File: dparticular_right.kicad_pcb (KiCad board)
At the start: 2 copper layers, 51 parts, among them J1 To Left Hand, SW1:10 Key_Ins, SW1:11 Key_Prnt, SW2:10 Key_F7, SW2:11 Key_F8, SW2:12 Key_F9, SW2:13 Key_F10, SW2:14 Key_F11, SW2:15 Key_F12, SW2:16 Key_Del, SW3:10 Key_7, SW3:11 Key_8, SW3:12 Key_9, SW3:13 Key_0, SW3:14 Key_Hyph, SW3:15 Key_Eql, SW3:16 Key_Bksp, SW3:9 Key_6, SW4:10 Key_U, SW4:11 Key_I, SW4:12 Key_O, SW4:13 Key_P, SW4:14 Key_LBrk, SW4:15 Key_RBrk, SW4:16 Key_BkSl, SW4:9 Key_Y, SW5:10 Key_J, SW5:11 Key_K, SW5:12 Key_L, SW5:13 Key_Semi, SW5:14 Key_Quot, SW5:16 Key_Entr, SW5:9 Key_H, SW6:10 Key_M, SW6:11 Key_Coma, SW6:12 Key_Per, SW6:13 Key_Slsh, SW6:14 Key_RShft, SW6:9 Key_N, SW7:11 Key_RAlt, SW7:12 Key_RWin, SW7:13 Key_Menu, SW7:14 Key_RCtrl, SW7:9 Key_RSpc, U1 MCP23018

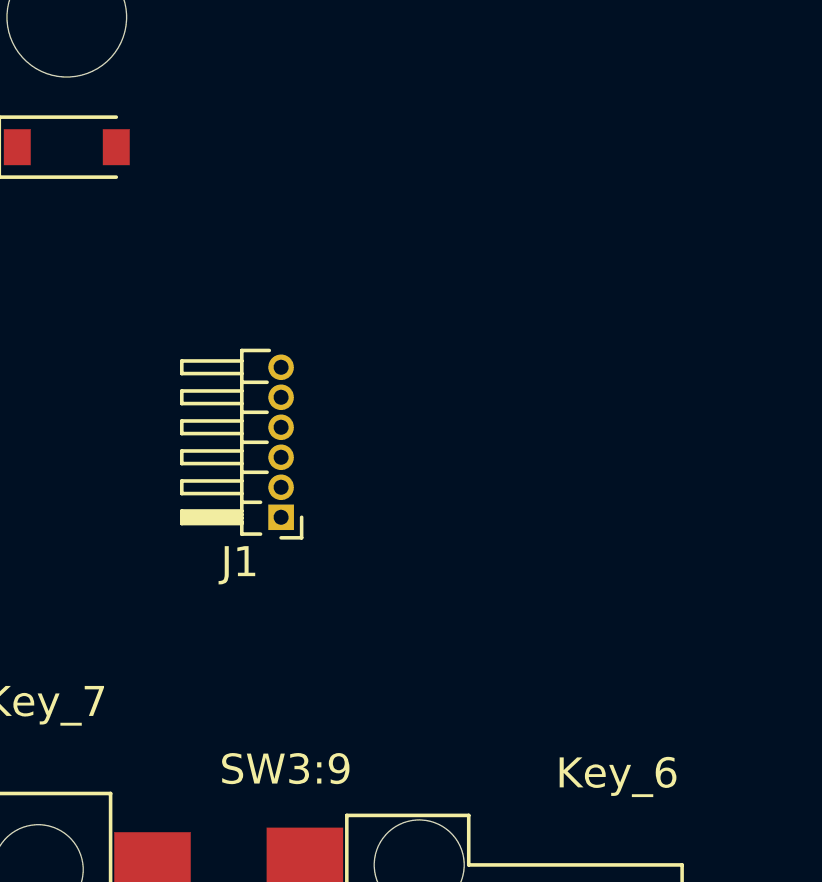
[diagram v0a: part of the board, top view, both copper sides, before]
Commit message: Fixed footprints on switches and headers
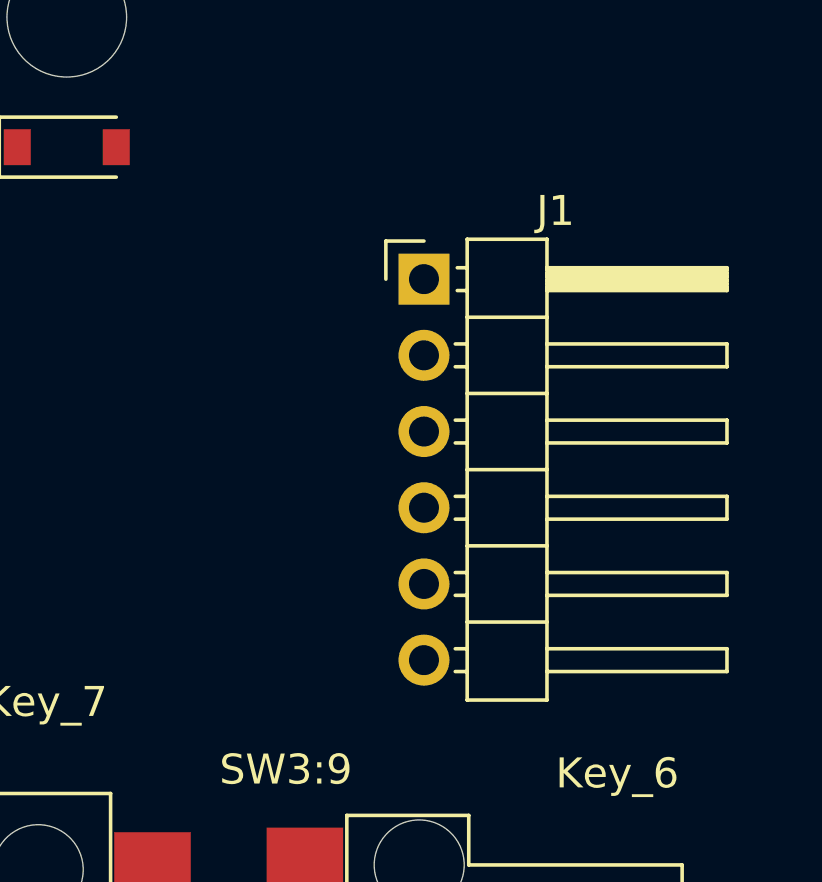
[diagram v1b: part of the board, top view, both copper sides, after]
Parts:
- J1: footprint Connector_PinHeader_1.00mm:PinHeader_1x06_P1.00mm_Horizontal -> Connector_PinHeader_2.54mm:PinHeader_1x06_P2.54mm_Horizontal
- moved J1 9.26 mm to (188.1, 65.9), turned to 0 degrees

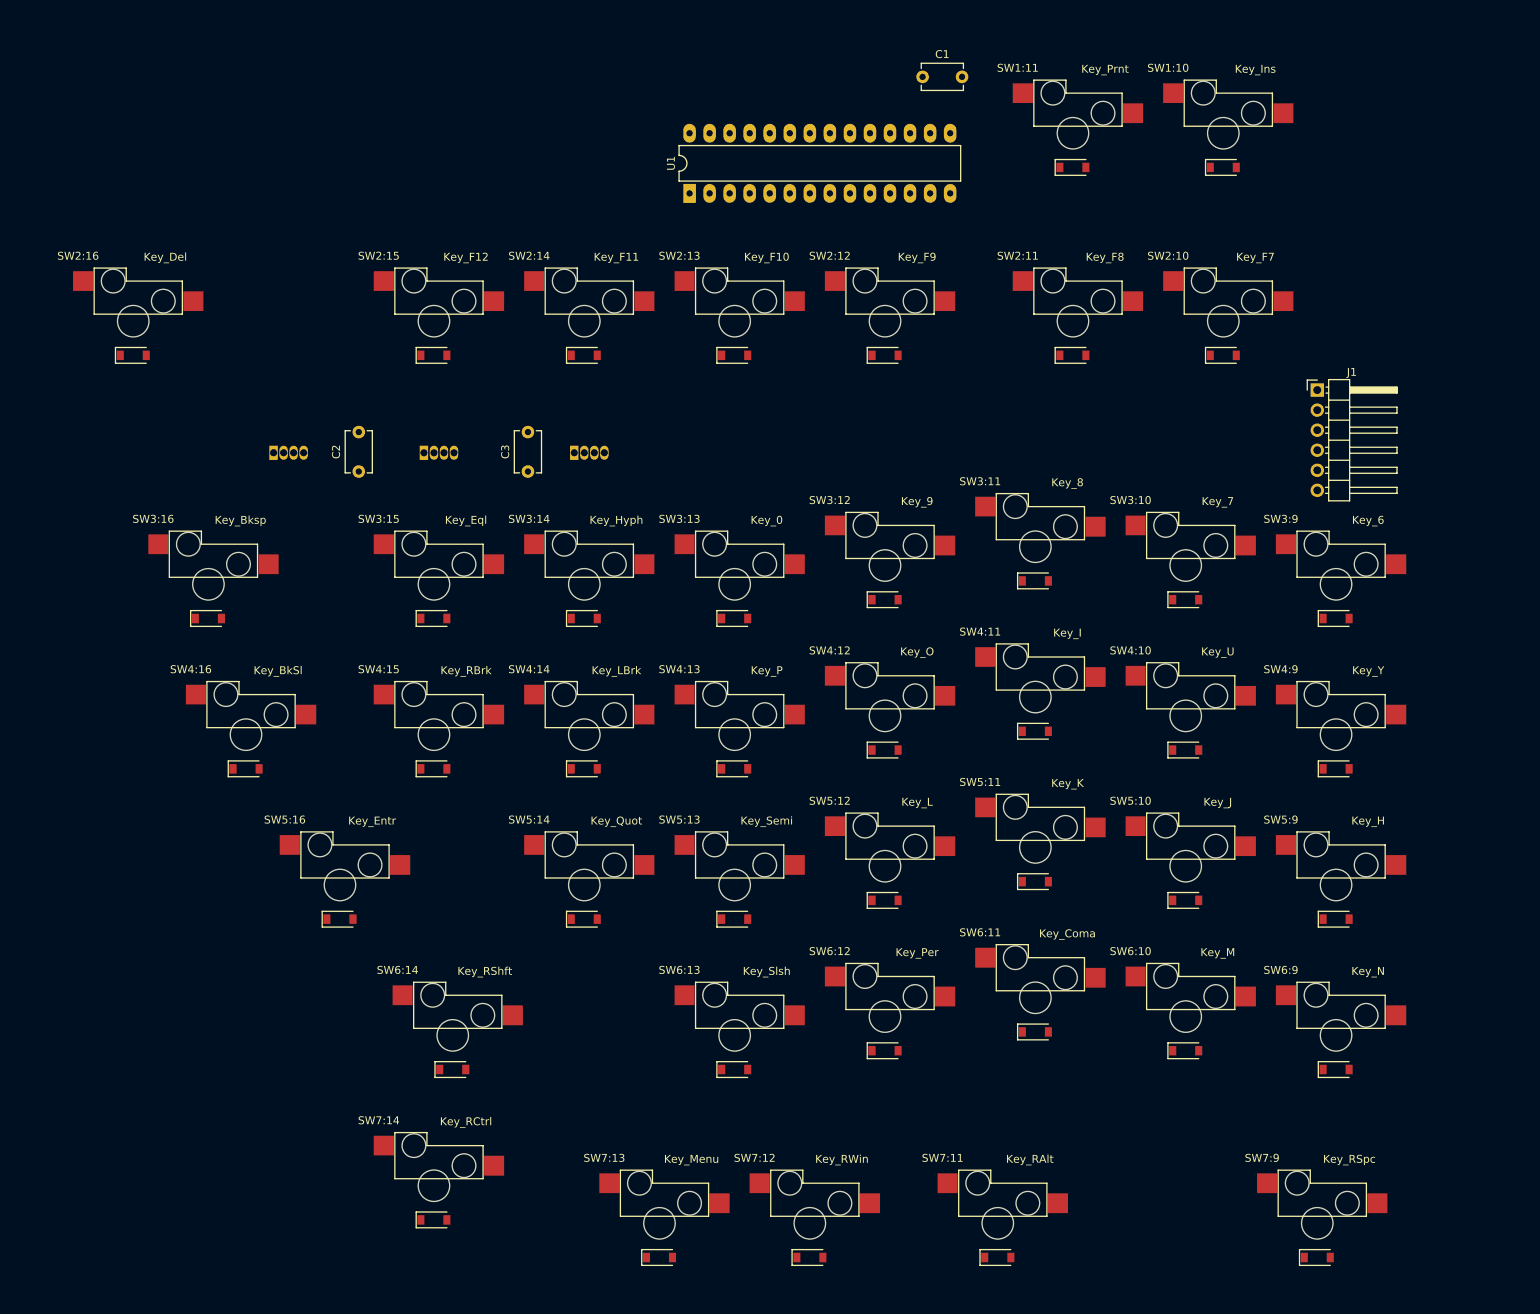
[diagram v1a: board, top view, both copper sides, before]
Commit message: Edge cuts, net list exports
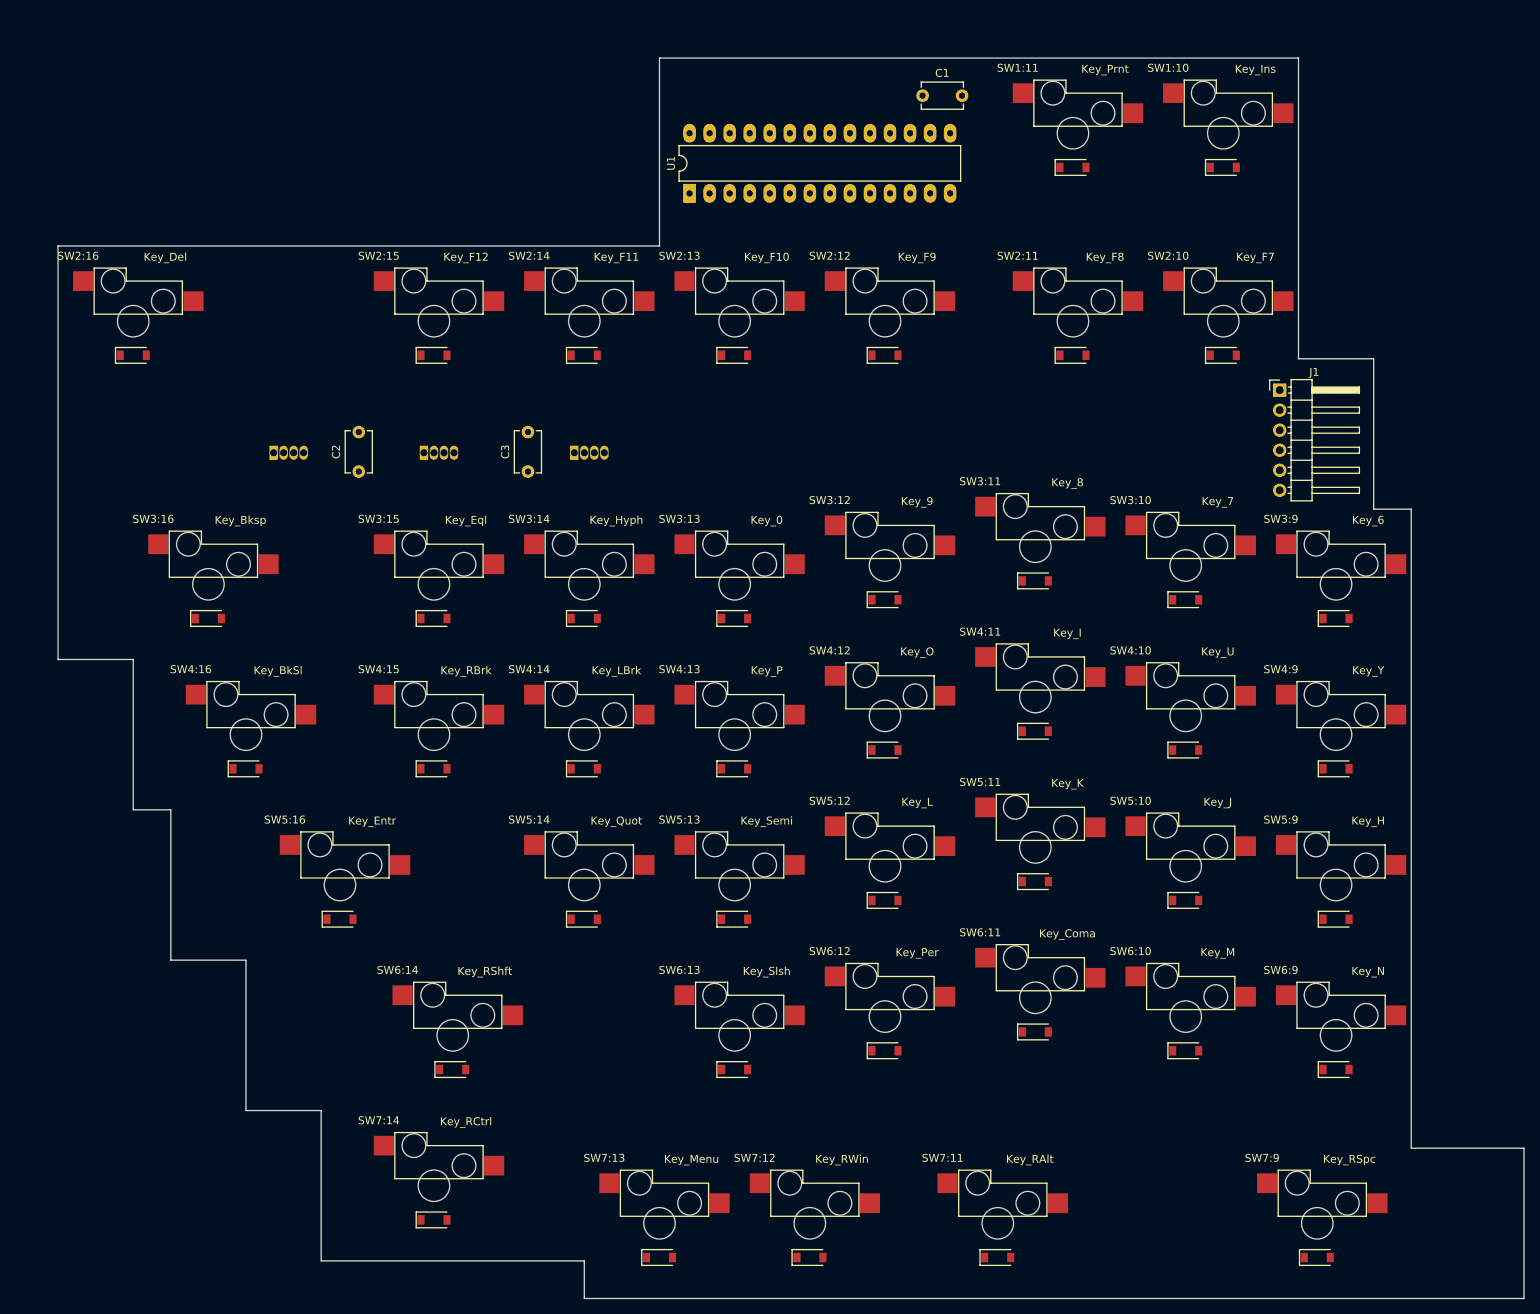
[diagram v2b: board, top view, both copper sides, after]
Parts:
- moved J1 4.76 mm to (183.4, 65.9)
- moved C1 2.38 mm to (138.1, 28.6)
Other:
- board outline added: 185.7 x 157.2 mm

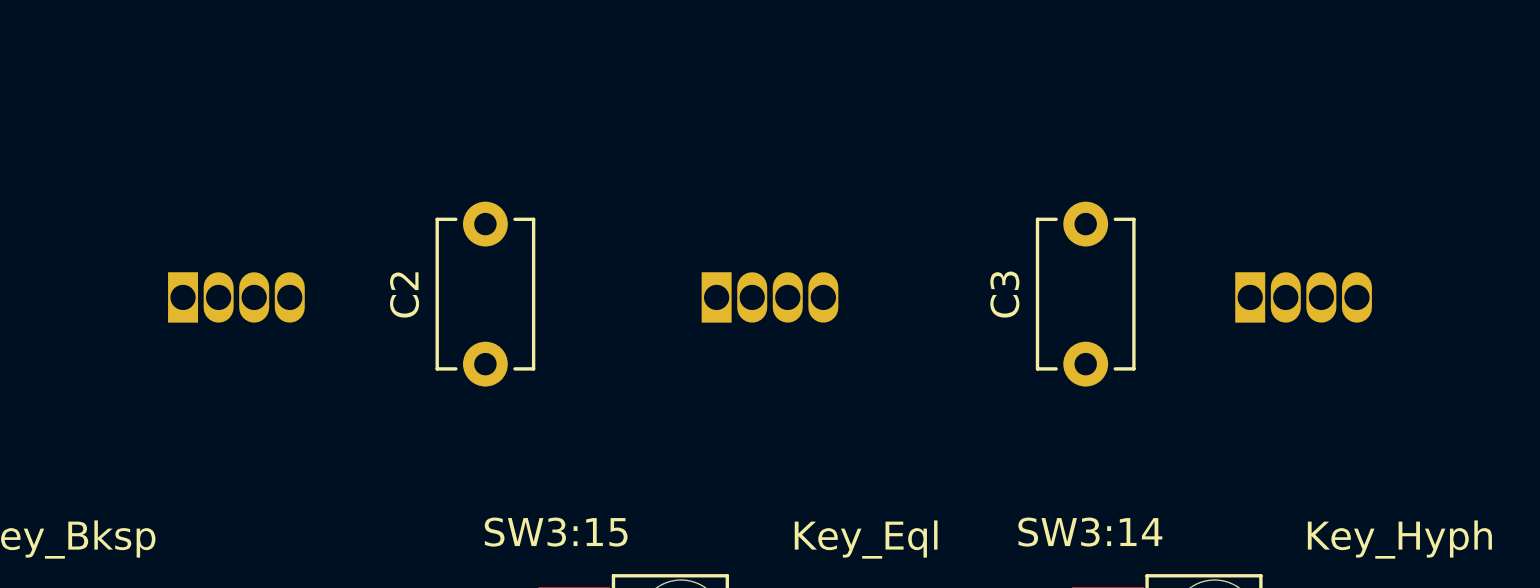
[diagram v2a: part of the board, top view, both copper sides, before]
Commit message: LED orientation and wiring
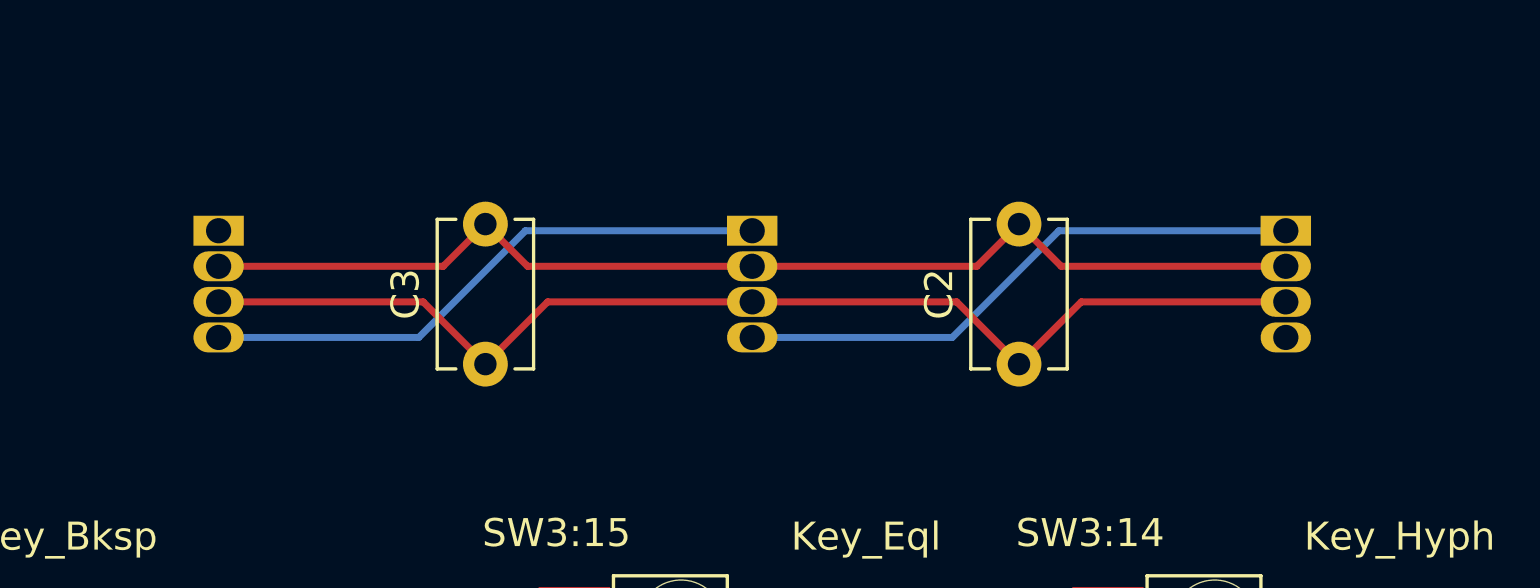
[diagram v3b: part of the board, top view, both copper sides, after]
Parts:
- moved D1 39.4 mm to (95.2, 71.4), turned to 270 degrees
- moved D3 36.9 mm to (57.1, 71.4), turned to 270 degrees
- moved C3 21.4 mm to (66.7, 76.2)
- moved C2 19.0 mm to (85.7, 76.2)
- moved D2 2.70 mm to (76.2, 71.4), turned to 270 degrees
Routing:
- net +5V: track 0.00 -> 41.8 mm
- net GND: track 0.00 -> 40.6 mm
- net Net-(D2-Pad1): track 0.00 -> 20.9 mm
- net Net-(D1-Pad1): track 0.00 -> 20.6 mm

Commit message: Design rules compatible with common prototype board manufacturers
Maximums that work with JLCPCB, ALLPCB, and Elecrow
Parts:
- D1: value APA-106-F5 -> NumLock
- D2: value APA-106-F5 -> CapsLock
- D3: value APA-106-F5 -> ScrollLock
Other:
- net class Default: clearance 0.2 -> 0.254; trace_width 0.25 -> 0.254; via_dia 0.8 -> 0.635; via_drill 0.4 -> 0.381
- rule trace_clearance: 0.2 -> 0.254
- rule trace_min: 0.2 -> 0.2032
- rule via_min_drill: 0.3 -> 0.254
- rule via_min_size: 0.4 -> 0.5588
